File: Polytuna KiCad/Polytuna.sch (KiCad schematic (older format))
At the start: 36 parts, among them IC1 AP7313-33SAG-7, SW1 SW_Push, SW2 SW_Push, SW3 SW_Push, SW4 SW_DPDT_x2, U1 LM358, U2 SGTL5000

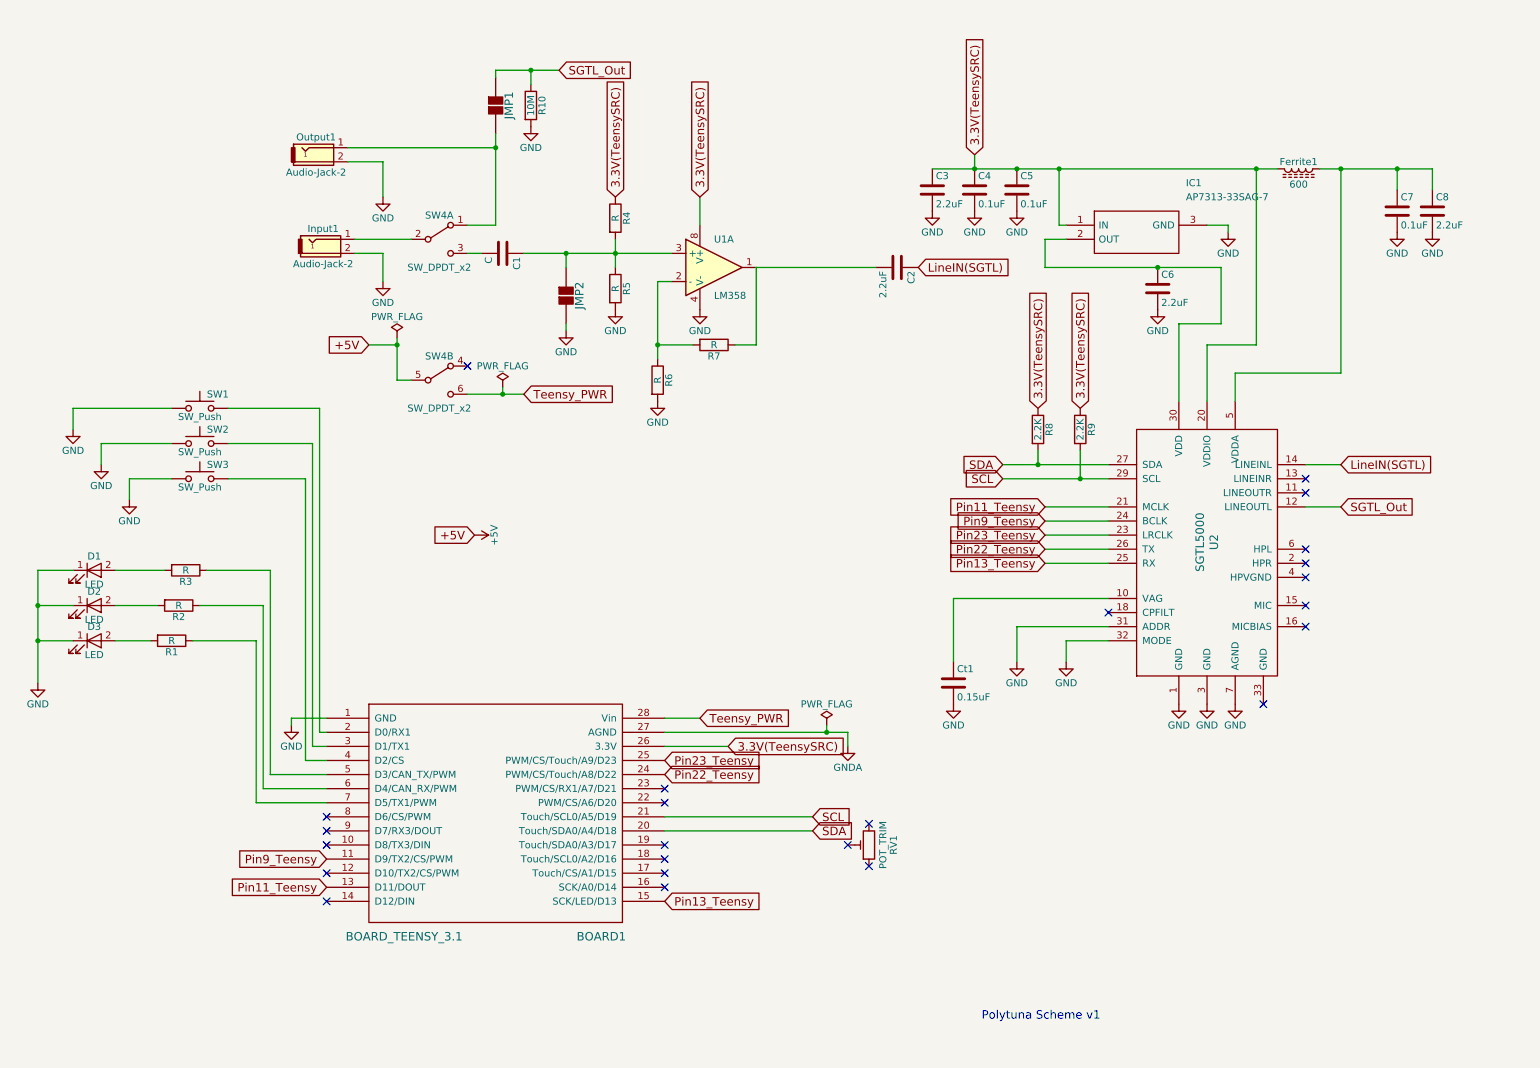
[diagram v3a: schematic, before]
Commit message: Added i2c ports to scheme and power stage
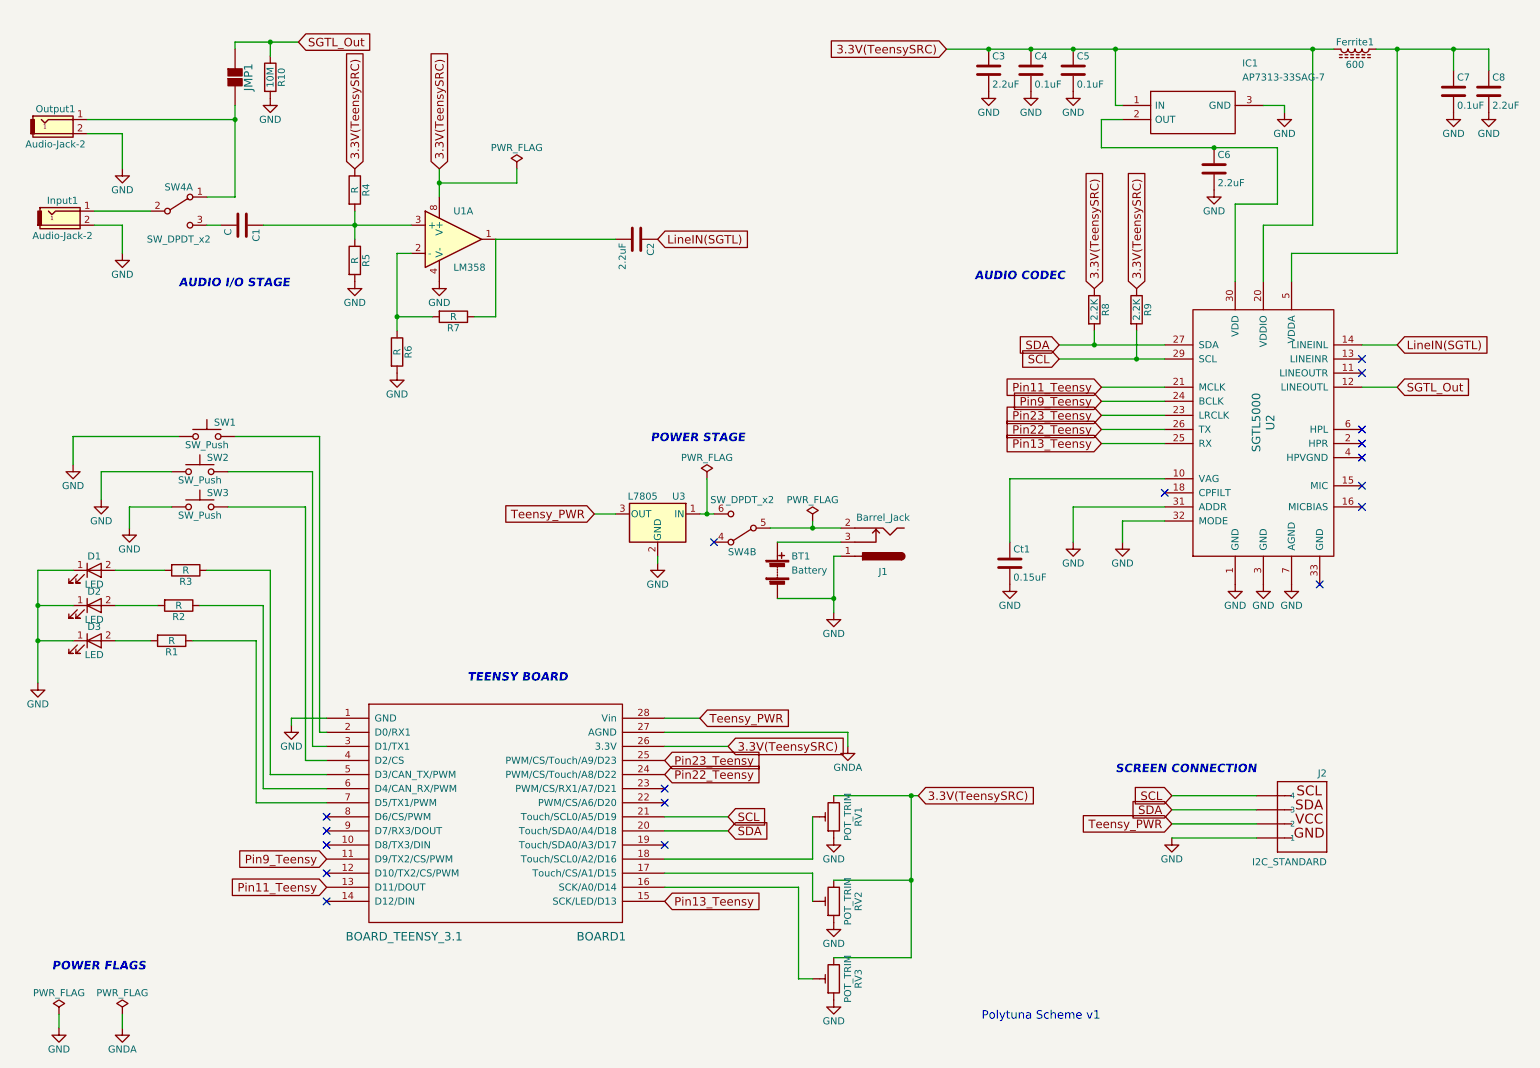
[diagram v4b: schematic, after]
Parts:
- removed JMP2: 2Jumper, symbol 2Jumper
- added BT1: Battery, symbol Battery
- added J1: Barrel_Jack, symbol Barrel_Jack
- added J2: I2C_STANDARD, SparkFun-Connectors_1X04, symbol I2C_STANDARD
- added RV2, RV3: POT_TRIM, symbol POT_TRIM
- added U3: L7805, symbol L7805
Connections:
- net 3.3V(TeensySRC): now also RV1.3, RV2.3, RV3.3
- net GND: now also RV1.1, BT1.2 (-), J1.1, J2.1, RV2.1, RV3.1, U3.2 (GND)
- net SCL: now also J2.4
- net SDA: now also J2.3
- net Teensy_PWR: now also J2.2, U3.3 (OUT); no longer SW4.6 (C)
- net at BOARD1.16 (SCK/A0/D14): now also RV3.2
- net at BOARD1.17 (Touch/CS/A1/D15): now also RV2.2
- net at BOARD1.18 (Touch/SCL0/A2/D16): now also RV1.2
- net +5V: no longer names the net of SW4.5 (B)
- net +5V: now also J1.2
- new net: SW4.6 (C), U3.1 (IN)
- new net: BT1.1 (+), J1.3
- no-connect marks 24 -> 18
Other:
- note added: "AUDIO CODEC\n"
- note added: "AUDIO I/O STAGE"
- note added: "POWER FLAGS"
- note added: "POWER STAGE"
- note added: "SCREEN CONNECTION"
- note added: "TEENSY BOARD \n"
- moved on the sheet: C1, C2, C3, C4, C5, C6, C7, C8, Ct1, Ferrite1, IC1, Input1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

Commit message: Solve power flag issues
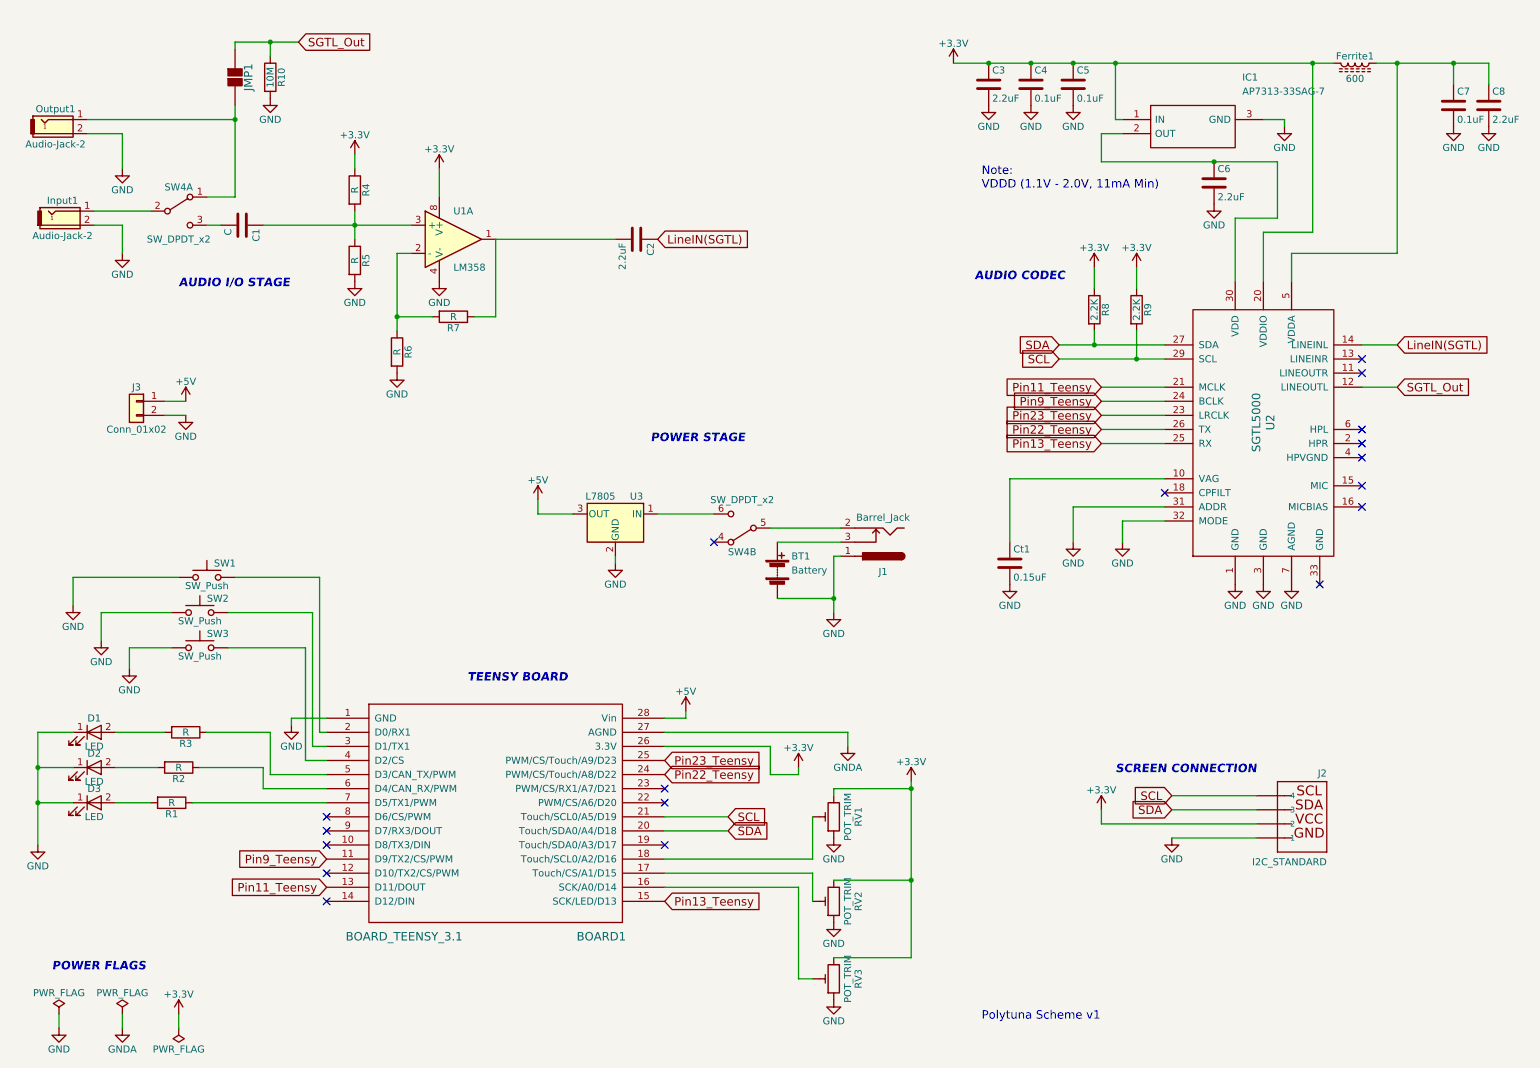
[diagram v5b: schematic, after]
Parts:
- added J3: Conn_01x02, symbol Conn_01x02
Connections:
- net GND: now also J3.2 (Pin_2)
- net 3.3V(TeensySRC) renamed +3V3
- net +3V3: now also J2.2
- net Teensy_PWR renamed +5V
- net +5V: now also J3.1 (Pin_1); no longer J2.2
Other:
- note added: "Note: \nVDDD (1.1V - 2.0V, 11mA Min)"
- moved on the sheet: C3, C4, C5, C6, C7, C8, D1, D2, D3, Ferrite1, IC1, R1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

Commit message: Corrected GNDA/GND and i2c pins
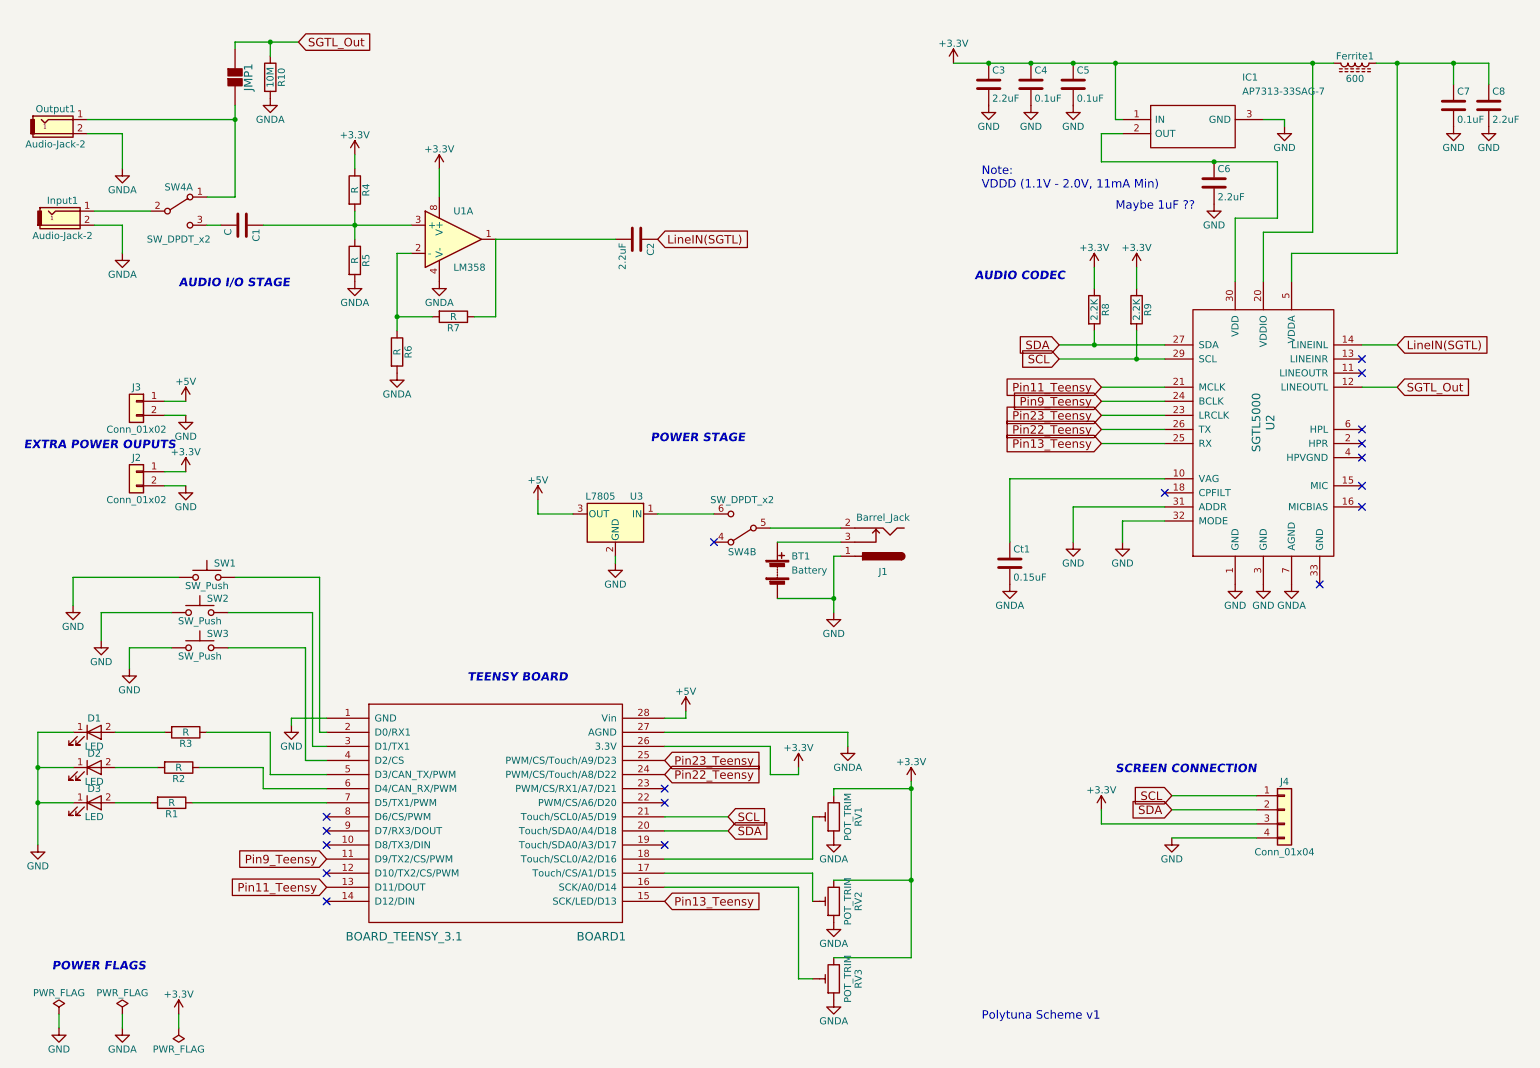
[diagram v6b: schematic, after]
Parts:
- removed J2: I2C_STANDARD, SparkFun-Connectors_1X04, symbol I2C_STANDARD
- added J2: Conn_01x02, symbol Conn_01x02
- added J4: Conn_01x04, symbol Conn_01x04
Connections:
- net +3V3: now also J2.1 (Pin_1), J4.3 (Pin_3)
- net GND: now also J2.2 (Pin_2), J4.4 (Pin_4); no longer Ct1.2, Input1.2, Output1.2, R10.2, R5.2, R6.2, RV1.1, RV2.1, RV3.1, U1.4 (V-), U2.7 (AGND)
- net GNDA: now also Ct1.2, Input1.2, Output1.2, R10.2, R5.2, R6.2, RV1.1, RV2.1, RV3.1, U1.4 (V-), U2.7 (AGND)
- net SCL: now also J4.1 (Pin_1)
- net SDA: now also J4.2 (Pin_2)
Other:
- note added: "EXTRA POWER OUPUTS"
- note added: "Maybe 1uF ??"

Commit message: Finished schematic
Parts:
- U3: symbol L7805 -> L7805-RESCUE-Polytuna
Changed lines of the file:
@@
 EESchema Schematic File Version 2
+LIBS:Polytuna-rescue
 LIBS:power
 LIBS:device
@@
 $EndComp
 $Comp
-L L7805 U3
+L L7805-RESCUE-Polytuna U3
 U 1 1 5AA245E8
 P 4750 3900

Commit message: Added some footprints
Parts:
- C1, C2, C3, C4, C5, C6, C7, C8, Ct1: footprint (none) -> Capacitors_SMD:C_0805
- Ferrite1: footprint (none) -> Inductors_SMD:L_0805
- IC1: footprint SOT96P240X110-3N -> (none)
- R1, R10, R2, R3, R4, R5, R6, R7, R8, R9: footprint (none) -> Resistors_SMD:R_0805
- U1: footprint (none) -> Housings_SOIC:SOIC-8-1EP_3.9x4.9mm_Pitch1.27mm
- U2: footprint (none) -> Housings_DFN_QFN:QFN-32-1EP_5x5mm_Pitch0.5mm
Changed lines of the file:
@@
 F 0 "R6" V 3280 2750 50  0000 C CNN
 F 1 "R" V 3200 2750 50  0000 C CNN
-F 2 "" V 3130 2750 50  0001 C CNN
+F 2 "Resistors_SMD:R_0805" V 3130 2750 50  0001 C CNN
 F 3 "" H 3200 2750 50  0001 C CNN
 	1    3200 2750
@@
 F 0 "R5" V 2980 2100 50  0000 C CNN
 F 1 "R" V 2900 2100 50  0000 C CNN
-F 2 "" V 2830 2100 50  0001 C CNN
+F 2 "Resistors_SMD:R_0805" V 2830 2100 50  0001 C CNN
 F 3 "" H 2900 2100 50  0001 C CNN
 	1    2900 2100
@@
 F 0 "R7" V 3680 2500 50  0000 C CNN
 F 1 "R" V 3600 2500 50  0000 C CNN
-F 2 "" V 3530 2500 50  0001 C CNN
+F 2 "Resistors_SMD:R_0805" V 3530 2500 50  0001 C CNN
 F 3 "" H 3600 2500 50  0001 C CNN
 	1    3600 2500
@@
 F 0 "R4" V 2980 1600 50  0000 C CNN
 F 1 "R" V 2900 1600 50  0000 C CNN
-F 2 "" V 2830 1600 50  0001 C CNN
+F 2 "Resistors_SMD:R_0805" V 2830 1600 50  0001 C CNN
 F 3 "" H 2900 1600 50  0001 C CNN
 	1    2900 1600
@@
 F 0 "C1" H 2125 1950 50  0000 L CNN
 F 1 "C" H 2125 1750 50  0000 L CNN
-F 2 "" H 2138 1700 50  0001 C CNN
+F 2 "Capacitors_SMD:C_0805" H 2138 1700 50  0001 C CNN
 F 3 "" H 2100 1850 50  0001 C CNN
 	1    2100 1850
@@
 F 0 "U1" H 3600 2150 50  0000 L CNN
 F 1 "LM358" H 3600 1750 50  0000 L CNN
-F 2 "" H 3600 1950 50  0001 C CNN
+F 2 "Housings_SOIC:SOIC-8-1EP_3.9x4.9mm_Pitch1.27mm" H 3600 1950 50  0001 C CNN
 F 3 "" H 3600 1950 50  0001 C CNN
 	1    3600 1950
@@
 F 0 "U2" V 9400 3350 60  0000 C CNN
 F 1 "SGTL5000" V 9300 3350 60  0000 C CNN
-F 2 "" H 9350 3350 60  0000 C CNN
+F 2 "Housings_DFN_QFN:QFN-32-1EP_5x5mm_Pitch0.5mm" H 9350 3350 60  0001 C CNN
 F 3 "" H 9350 3350 60  0000 C CNN
 	1    9350 3300
@@
 F 0 "C2" H 4925 2050 50  0000 L CNN
 F 1 "2.2uF" H 4925 1850 50  0000 L CNN
-F 2 "" H 4938 1800 50  0001 C CNN
+F 2 "Capacitors_SMD:C_0805" H 4938 1800 50  0001 C CNN
 F 3 "" H 4900 1950 50  0001 C CNN
 	1    4900 1950
@@
 F 0 "Ct1" H 7575 4350 50  0000 L CNN
 F 1 "0.15uF" H 7575 4150 50  0000 L CNN
-F 2 "" H 7588 4100 50  0001 C CNN
+F 2 "Capacitors_SMD:C_0805" H 7588 4100 50  0001 C CNN
 F 3 "" H 7550 4250 50  0001 C CNN
 	1    7550 4250
@@
 F 0 "R8" V 8230 2450 50  0000 C CNN
 F 1 "2.2K" V 8150 2450 50  0000 C CNN
-F 2 "" V 8080 2450 50  0001 C CNN
+F 2 "Resistors_SMD:R_0805" V 8080 2450 50  0001 C CNN
 F 3 "" H 8150 2450 50  0001 C CNN
 	1    8150 2450
@@
 F 0 "R9" V 8530 2450 50  0000 C CNN
 F 1 "2.2K" V 8450 2450 50  0000 C CNN
-F 2 "" V 8380 2450 50  0001 C CNN
+F 2 "Resistors_SMD:R_0805" V 8380 2450 50  0001 C CNN
 F 3 "" H 8450 2450 50  0001 C CNN
 	1    8450 2450
@@
 F 0 "C8" H 10975 1100 50  0000 L CNN
 F 1 "2.2uF" H 10975 900 50  0000 L CNN
-F 2 "" H 10988 850 50  0001 C CNN
+F 2 "Capacitors_SMD:C_0805" H 10988 850 50  0001 C CNN
 F 3 "" H 10950 1000 50  0001 C CNN
 	1    10950 1000
@@
 F 0 "C6" H 9025 1650 50  0000 L CNN
 F 1 "2.2uF" H 9025 1450 50  0000 L CNN
-F 2 "" H 9038 1400 50  0001 C CNN
+F 2 "Capacitors_SMD:C_0805" H 9038 1400 50  0001 C CNN
 F 3 "" H 9000 1550 50  0001 C CNN
 	1    9000 1550
@@
 F 0 "C3" H 7425 950 50  0000 L CNN
 F 1 "2.2uF" H 7425 750 50  0000 L CNN
-F 2 "" H 7438 700 50  0001 C CNN
+F 2 "Capacitors_SMD:C_0805" H 7438 700 50  0001 C CNN
 F 3 "" H 7400 850 50  0001 C CNN
 	1    7400 850
@@
 F 0 "C7" H 10725 1100 50  0000 L CNN
 F 1 "0.1uF" H 10725 900 50  0000 L CNN
-F 2 "" H 10738 850 50  0001 C CNN
+F 2 "Capacitors_SMD:C_0805" H 10738 850 50  0001 C CNN
 F 3 "" H 10700 1000 50  0001 C CNN
 	1    10700 1000
@@
 F 0 "C4" H 7725 950 50  0000 L CNN
 F 1 "0.1uF" H 7725 750 50  0000 L CNN
-F 2 "" H 7738 700 50  0001 C CNN
+F 2 "Capacitors_SMD:C_0805" H 7738 700 50  0001 C CNN
 F 3 "" H 7700 850 50  0001 C CNN
 	1    7700 850
@@
 F 0 "C5" H 8025 950 50  0000 L CNN
 F 1 "0.1uF" H 8025 750 50  0000 L CNN
-F 2 "" H 8038 700 50  0001 C CNN
+F 2 "Capacitors_SMD:C_0805" H 8038 700 50  0001 C CNN
 F 3 "" H 8000 850 50  0001 C CNN
 	1    8000 850
@@
 F 0 "Ferrite1" V 9950 700 50  0000 C CNN
 F 1 "600" V 10110 700 50  0000 C CNN
-F 2 "" H 10000 700 50  0001 C CNN
+F 2 "Inductors_SMD:L_0805" H 10000 700 50  0001 C CNN
 F 3 "" H 10000 700 50  0001 C CNN
 	1    10000 700
@@
 F 0 "BOARD1" H 4650 5000 60  0000 C CNN
 F 1 "BOARD_TEENSY_3.1" H 3250 5000 60  0000 C CNN
-F 2 "" H 3900 4850 60  0000 C CNN
+F 2 "" H 3900 4850 60  0001 C CNN
 F 3 "" H 3900 4850 60  0000 C CNN
 	1    3900 5950
@@
 F 0 "JMP1" H 2050 895 60  0000 C CNN
 F 1 "2Jumper" H 2050 985 60  0001 C CNN
-F 2 "" H 3205 870 60  0000 C CNN
+F 2 "" H 3205 870 60  0001 C CNN
 F 3 "" H 3205 870 60  0000 C CNN
 	1    2050 800
@@
 F 0 "R3" V 1780 5450 50  0000 C CNN
 F 1 "R" V 1700 5450 50  0000 C CNN
-F 2 "" V 1630 5450 50  0001 C CNN
+F 2 "Resistors_SMD:R_0805" V 1630 5450 50  0001 C CNN
 F 3 "" H 1700 5450 50  0001 C CNN
 	1    1700 5450
@@
 F 0 "R2" V 1730 5700 50  0000 C CNN
 F 1 "R" V 1650 5700 50  0000 C CNN
-F 2 "" V 1580 5700 50  0001 C CNN
+F 2 "Resistors_SMD:R_0805" V 1580 5700 50  0001 C CNN
 F 3 "" H 1650 5700 50  0001 C CNN
 	1    1650 5700
@@
 F 0 "R1" V 1680 5950 50  0000 C CNN
 F 1 "R" V 1600 5950 50  0000 C CNN
-F 2 "" V 1530 5950 50  0001 C CNN
+F 2 "Resistors_SMD:R_0805" V 1530 5950 50  0001 C CNN
 F 3 "" H 1600 5950 50  0001 C CNN
 	1    1600 5950
@@
 F 0 "R10" V 2380 800 50  0000 C CNN
 F 1 "10M" V 2300 800 50  0000 C CNN
-F 2 "" V 2230 800 50  0001 C CNN
+F 2 "Resistors_SMD:R_0805" V 2230 800 50  0001 C CNN
 F 3 "" H 2300 800 50  0001 C CNN
 	1    2300 800
@@
 F 0 "IC1" H 9200 1400 50  0000 L CNN
 F 1 "AP7313-33SAG-7" H 9200 1300 50  0000 L CNN
-F 2 "SOT96P240X110-3N" H 9200 1200 50  0001 L CNN
+F 2 "" H 9200 1200 50  0001 L CNN
 F 3 "https://componentsearchengine.com/Datasheets/1/AP7313-33SAG-7.pdf" H 9200 1100 50  0001 L CNN
 F 4 "Diodes Inc AP7313-33SAG-7, Single Linear Voltage Regulator, 150mA 3.3 V, 2%, 3-Pin SOT-23" H 9200 1000 50  0001 L CNN "Description"
